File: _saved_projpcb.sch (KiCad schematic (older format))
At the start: 21 parts, among them CON1 BARREL_JACK, CON2 BARREL_JACK, P1 CONN_01X02, P2 CONN_01X02, P3 CONN_02X05, P4 CONN_02X05, Q16 Q_NMOS_GSD, U1 Teensy_3.1, U2 LM358, U3 CD74HC4067, U4 CL520

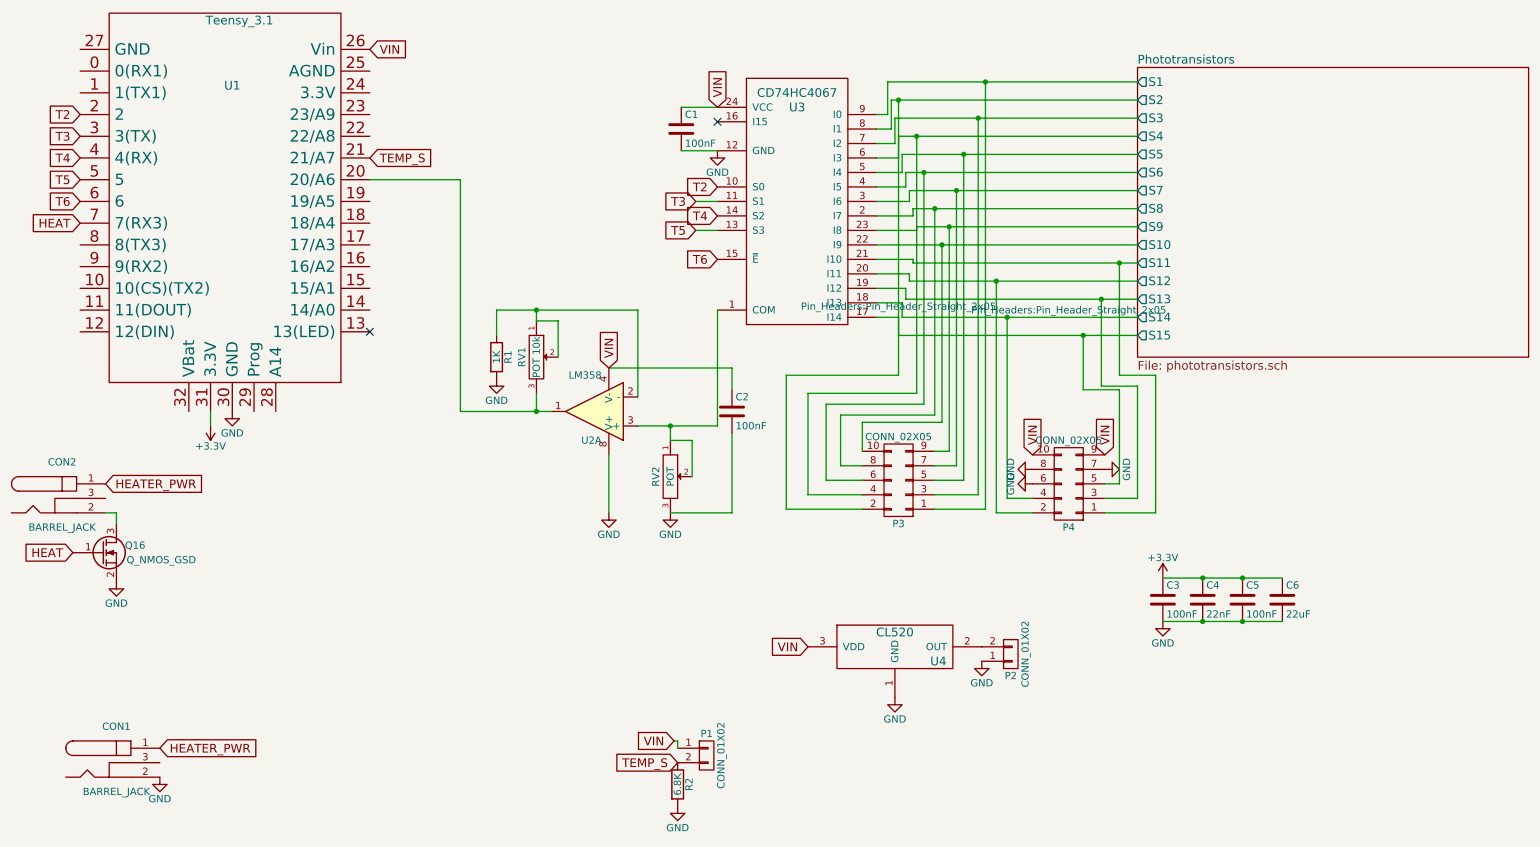
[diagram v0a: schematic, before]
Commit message: Added breakout headers for phototransistors, added GNDA for analog aspects
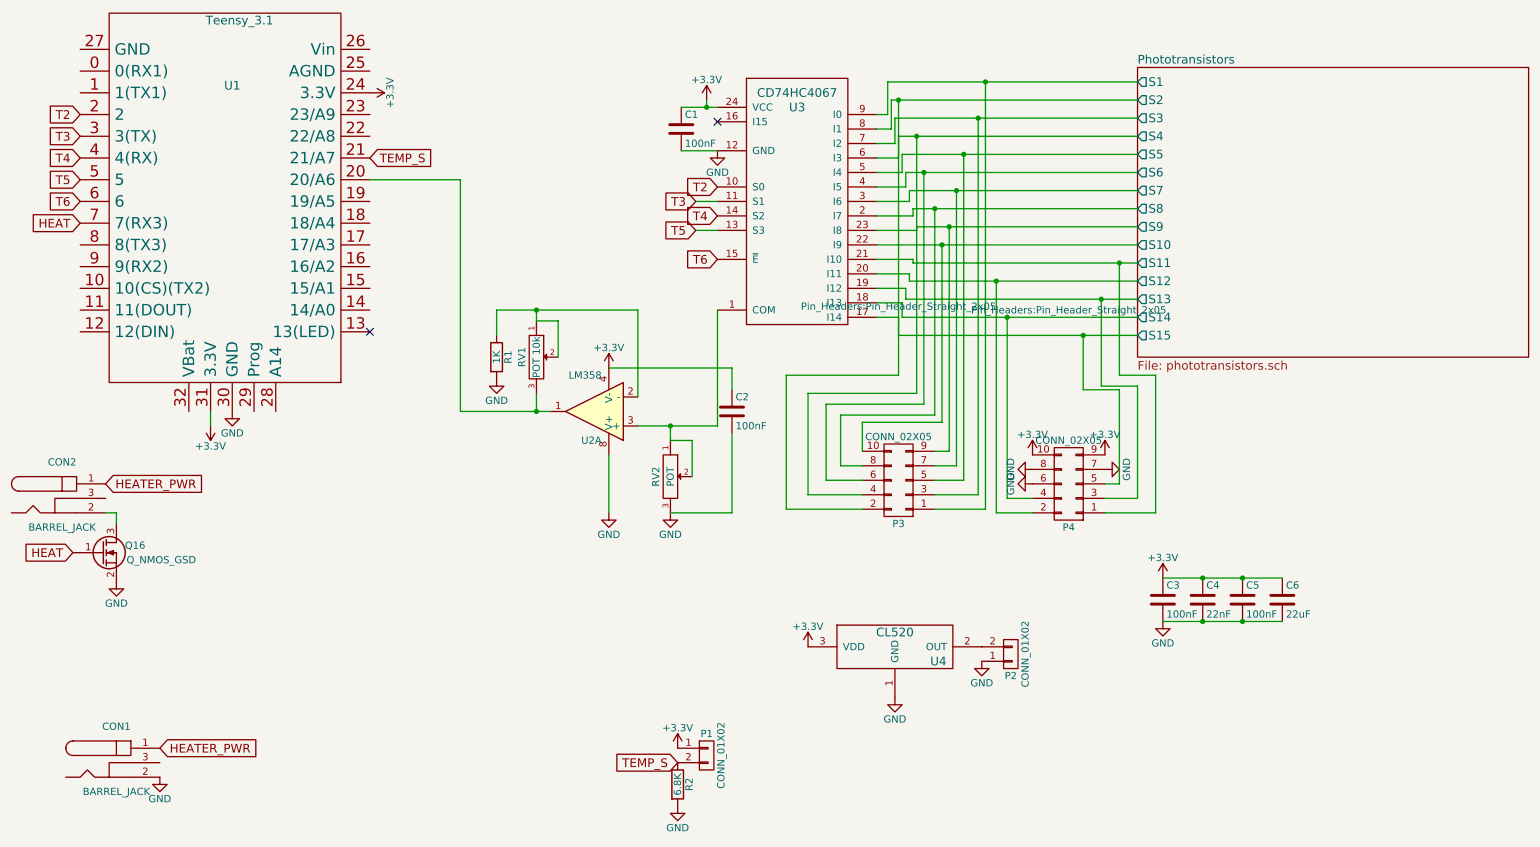
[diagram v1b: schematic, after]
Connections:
- net +3V3: now also C1.1, C2.1, P1.1 (P1), P4.10 (P10), P4.9 (P9), U1.24 (3.3V), U2.4 (V-), U3.24 (VCC), U4.3 (VDD)
- removed net VIN: C1.1, C2.1, P1.1 (P1), P4.10 (P10), P4.9 (P9), U1.26 (Vin), U2.4 (V-), U3.24 (VCC), U4.3 (VDD)
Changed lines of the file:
@@
 	1    0    0    -1
 $EndComp
-Text GLabel 4675 3350 1    60   Input ~ 0
-VIN
-Text GLabel 3025 1150 2    60   Input ~ 0
-VIN
 $Comp
 L POT RV1
@@
 	1    0    0    -1
 $EndComp
-Text GLabel 5425 1550 1    60   Input ~ 0
-VIN
 Text GLabel 1025 1600 0    60   Input ~ 0
 T2
@@
 Text GLabel 5150 6075 0    60   Input ~ 0
 TEMP_S
-Text GLabel 5125 5925 0    60   Input ~ 0
-VIN
 $Comp
 L CL520 U4
@@
 	1    0    0    -1
 $EndComp
-Text GLabel 6050 5275 0    60   Input ~ 0
-VIN
 $Comp
 L CONN_01X02 P2
@@
 	1275 4350 1200 4350
 Wire Wire Line
-	5125 5925 5150 5925
-Wire Wire Line
-	5150 5925 5150 5975
-Wire Wire Line
 	7275 1375 7275 4325
 Connection ~ 7275 1375
@@
 	7950 3500 7950 3125
 Connection ~ 7950 3125
-Text GLabel 7600 3950 1    60   Input ~ 0
-VIN
-Text GLabel 8100 3950 1    60   Input ~ 0
-VIN
 $Comp
 L GND #PWR12
@@
 	0    -1   -1   0
 $EndComp
+$Comp
+L +3.3V #PWR?
+U 1 1 56C854BA
+P 8100 3950
+F 0 "#PWR?" H 8100 3800 50  0001 C CNN
+F 1 "+3.3V" H 8100 4090 50  0000 C CNN
+F 2 "" H 8100 3950 50  0000 C CNN
+F 3 "" H 8100 3950 50  0000 C CNN
+	1    8100 3950
+	1    0    0    -1
+$EndComp
+$Comp
+L +3.3V #PWR?
+U 1 1 56C85644
+P 7600 3950
+F 0 "#PWR?" H 7600 3800 50  0001 C CNN
+F 1 "+3.3V" H 7600 4090 50  0000 C CNN
+F 2 "" H 7600 3950 50  0000 C CNN
+F 3 "" H 7600 3950 50  0000 C CNN
+	1    7600 3950
+	1    0    0    -1
+$EndComp
+$Comp
+L +3.3V #PWR?
+U 1 1 56C856E8
+P 5350 1500
+F 0 "#PWR?" H 5350 1350 50  0001 C CNN
+F 1 "+3.3V" H 5350 1640 50  0000 C CNN
+F 2 "" H 5350 1500 50  0000 C CNN
+F 3 "" H 5350 1500 50  0000 C CNN
+	1    5350 1500
+	1    0    0    -1
+$EndComp
+Wire Wire Line
+	5350 1500 5350 1550
+Connection ~ 5350 1550
+$Comp
+L +3.3V #PWR?
+U 1 1 56C86F91
+P 3025 1450
+F 0 "#PWR?" H 3025 1300 50  0001 C CNN
+F 1 "+3.3V" H 3025 1590 50  0000 C CNN
+F 2 "" H 3025 1450 50  0000 C CNN
+F 3 "" H 3025 1450 50  0000 C CNN
+	1    3025 1450
+	0    1    1    0
+$EndComp
+$Comp
+L +3.3V #PWR?
+U 1 1 56C888B3
+P 4675 3350
+F 0 "#PWR?" H 4675 3200 50  0001 C CNN
+F 1 "+3.3V" H 4675 3490 50  0000 C CNN
+F 2 "" H 4675 3350 50  0000 C CNN
+F 3 "" H 4675 3350 50  0000 C CNN
+	1    4675 3350
+	1    0    0    -1
+$EndComp
+$Comp
+L +3.3V #PWR?
+U 1 1 56C89220
+P 6050 5275
+F 0 "#PWR?" H 6050 5125 50  0001 C CNN
+F 1 "+3.3V" H 6050 5415 50  0000 C CNN
+F 2 "" H 6050 5275 50  0000 C CNN
+F 3 "" H 6050 5275 50  0000 C CNN
+	1    6050 5275
+	1    0    0    -1
+$EndComp
+$Comp
+L +3.3V #PWR?
+U 1 1 56C892C4
+P 5150 5975
+F 0 "#PWR?" H 5150 5825 50  0001 C CNN
+F 1 "+3.3V" H 5150 6115 50  0000 C CNN
+F 2 "" H 5150 5975 50  0000 C CNN
+F 3 "" H 5150 5975 50  0000 C CNN
+	1    5150 5975
+	1    0    0    -1
+$EndComp
 $EndSCHEMATC
